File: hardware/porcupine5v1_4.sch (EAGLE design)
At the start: 45 parts, among them X1 PROGCON

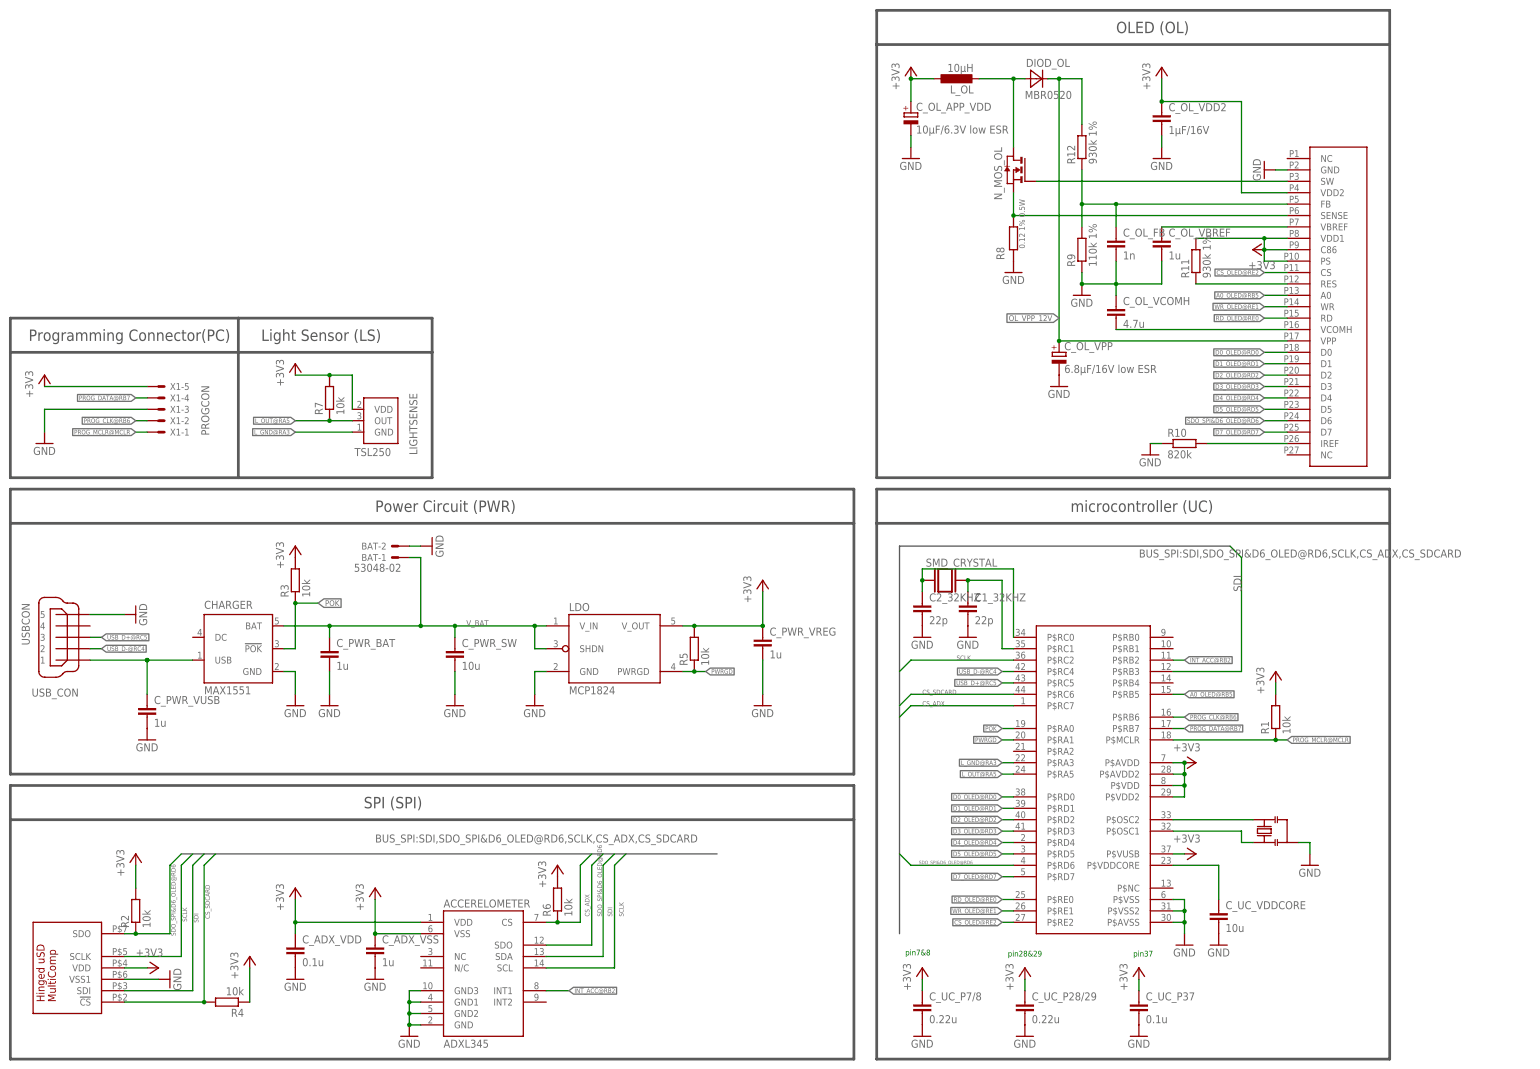
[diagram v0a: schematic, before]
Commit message: updated hedgehog library and next iteration versions
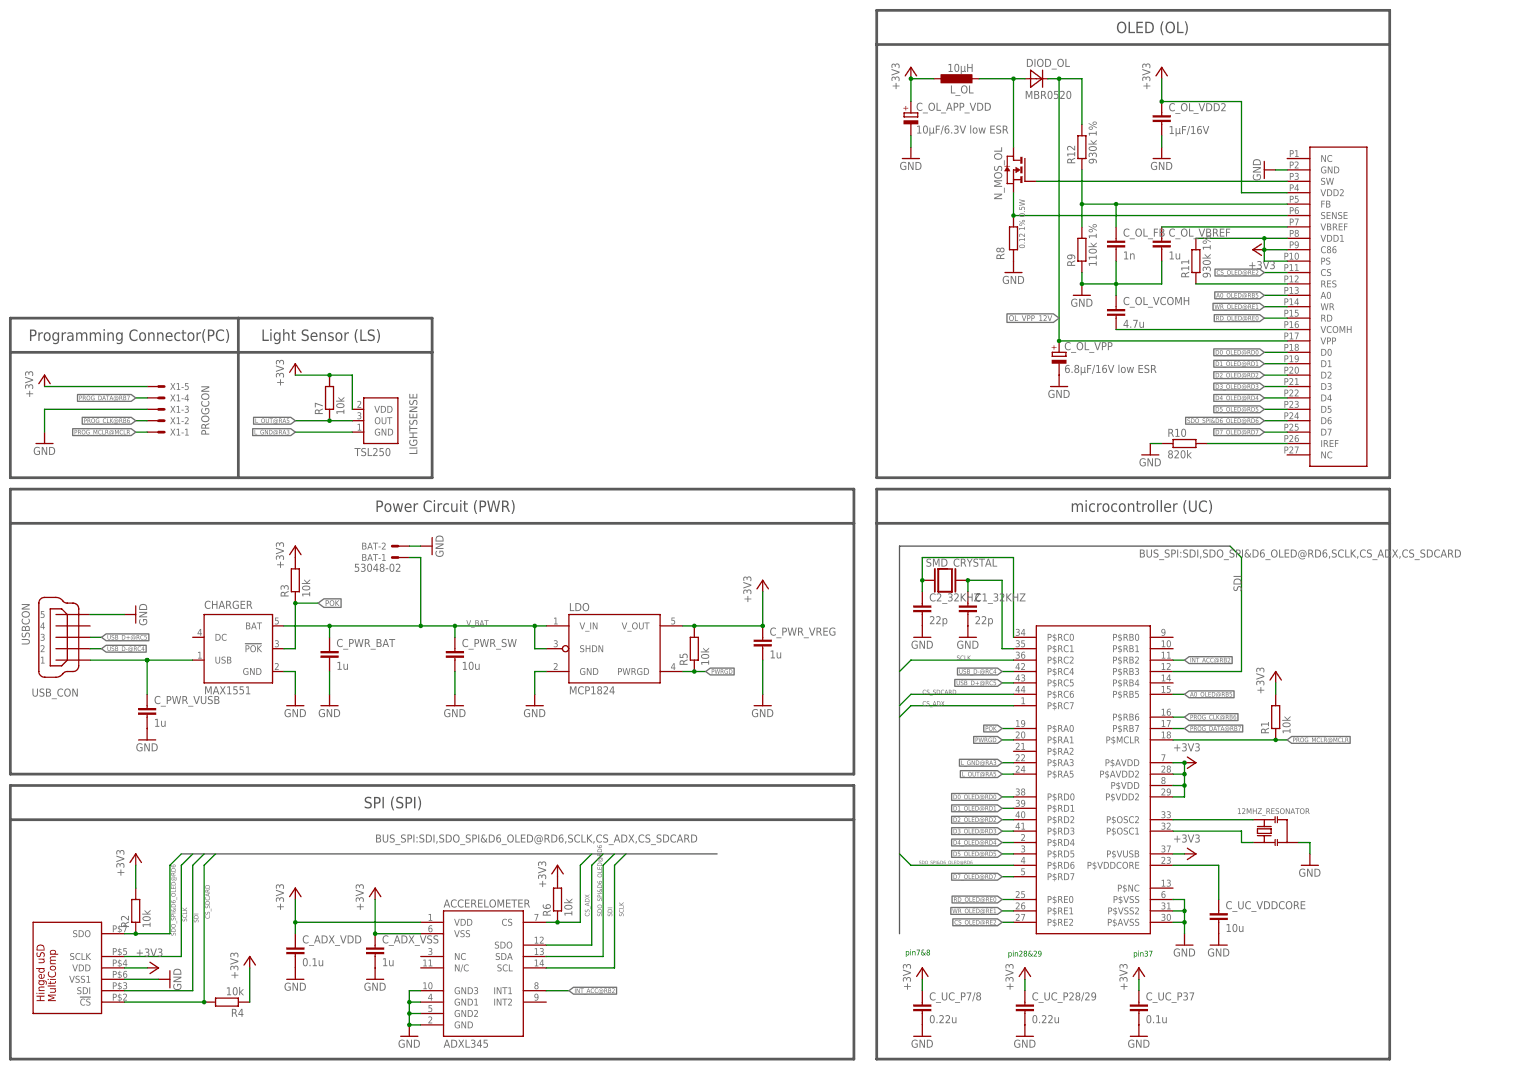
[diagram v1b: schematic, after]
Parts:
- renumbered U$1 to 12MHZ_RESONATOR
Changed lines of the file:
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@@
 <part name="R7" library="rcl" deviceset="R-EU_" device="R0603" value="10k"/>
 <part name="GND18" library="supply1" deviceset="GND" device=""/>
-<part name="U$1" library="HedgehogLib" deviceset="RESONATOR" device="PRQC-C"/>
+<part name="12MHZ_RESONATOR" library="HedgehogLib" deviceset="RESONATOR" device="PRQC-C"/>
 </parts>
 <sheets>
@@
 <instances>
 <instance part="GND3" gate="1" x="12.7" y="139.7"/>
-<instance part="SDCARD_CON" gate="G$1" x="30.48" y="25.4" smashed="yes" rot="R90"/>
+<instance part="SDCARD_CON" gate="G$1" x="17.78" y="22.86" smashed="yes" rot="R90"/>
 <instance part="GND16" gate="1" x="40.64" y="20.32" rot="R90"/>
 <instance part="LIGHTSENSE" gate="G$1" x="86.36" y="144.78" smashed="yes">
@@
 <instance part="R7" gate="G$1" x="76.2" y="149.86" rot="R90"/>
 <instance part="GND18" gate="1" x="284.48" y="200.66" rot="R270"/>
-<instance part="U$1" gate="RESONATOR" x="284.48" y="53.34" rot="R180"/>
+<instance part="12MHZ_RESONATOR" gate="RESONATOR" x="284.48" y="53.34" smashed="yes" rot="R180">
+<attribute name="NAME" x="294.64" y="58.42" size="1.27" layer="95" rot="R180"/>
+</instance>
 </instances>
 <busses>
@@
 <wire x1="292.1" y1="50.8" x2="294.64" y2="50.8" width="0.1524" layer="91"/>
 <wire x1="294.64" y1="50.8" x2="294.64" y2="48.26" width="0.1524" layer="91"/>
-<pinref part="U$1" gate="RESONATOR" pin="GND"/>
+<pinref part="12MHZ_RESONATOR" gate="RESONATOR" pin="GND"/>
 </segment>
 <segment>
@@
 <net name="N$3" class="0">
 <segment>
-<wire x1="208.28" y1="109.22" x2="208.28" y2="111.76" width="0.1524" layer="91"/>
-<wire x1="208.28" y1="111.76" x2="228.6" y2="111.76" width="0.1524" layer="91"/>
-<wire x1="228.6" y1="111.76" x2="228.6" y2="96.52" width="0.1524" layer="91"/>
+<wire x1="208.28" y1="109.22" x2="208.28" y2="114.3" width="0.1524" layer="91"/>
+<wire x1="208.28" y1="114.3" x2="228.6" y2="114.3" width="0.1524" layer="91"/>
+<wire x1="228.6" y1="114.3" x2="228.6" y2="96.52" width="0.1524" layer="91"/>
 <pinref part="C2_32KHZ" gate="G$1" pin="1"/>
 <pinref part="PIC_CONTROLLER" gate="G$1" pin="P$RC0"/>
@@
 <pinref part="PIC_CONTROLLER" gate="G$1" pin="P$OSC2"/>
 <wire x1="264.16" y1="55.88" x2="281.94" y2="55.88" width="0.1524" layer="91"/>
-<pinref part="U$1" gate="RESONATOR" pin="1"/>
+<pinref part="12MHZ_RESONATOR" gate="RESONATOR" pin="1"/>
 </segment>
 </net>
@@
 <pinref part="PIC_CONTROLLER" gate="G$1" pin="P$OSC1"/>
 <wire x1="279.4" y1="53.34" x2="264.16" y2="53.34" width="0.1524" layer="91"/>
-<pinref part="U$1" gate="RESONATOR" pin="2"/>
-</segment>
-</net>
+<pinref part="12MHZ_RESONATOR" gate="RESONATOR" pin="2"/>
+</segment>
+</net>
